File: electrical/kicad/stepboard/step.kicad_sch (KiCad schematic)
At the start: 80 parts, among them J1 Conn_02x03_Odd_Even, J10 Conn_02x03_Odd_Even, J11 Conn_02x03_Odd_Even, J12 Conn_02x03_Odd_Even, J13 Conn_01x04, J14 Conn_01x04, J15 Conn_01x04, J16 Conn_01x04, J17 Conn_02x03_Odd_Even, J18 Conn_02x03_Odd_Even, J19 Conn_02x03_Odd_Even, J2 Conn_02x03_Odd_Even, J20 Conn_02x03_Odd_Even, J21 Conn_01x04, J22 Conn_01x04, J23 Conn_01x04, J24 Conn_01x04, J25 Conn_02x12_Odd_Even, J26 Screw_Terminal_01x03, J3 Conn_02x03_Odd_Even, J4 Conn_02x03_Odd_Even, J5 Conn_01x04, J6 Conn_01x04, J7 Conn_01x04, J8 Conn_01x04, J9 Conn_02x03_Odd_Even, U1 MKS_TMC2209, U10 MKS_TMC2209, U11 MKS_TMC2209, U12 MKS_TMC2209, U2 MKS_TMC2209, U3 MKS_TMC2209, U4 MKS_TMC2209, U5 MKS_TMC2209, U6 MKS_TMC2209, U7 MKS_TMC2209, U8 MKS_TMC2209, U9 MKS_TMC2209

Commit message: update(kicad/pdb): sch with mobility components
- added rover mobility components to schematic
- added overcurrent and flyback protection ckt
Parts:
- renumbered J18 to J10, J19 to J11, J20 to J12, J5 to J13, J6 to J14, J7 to J15, J8 to J16, J13 to J17, J14 to J18, J15 to J19, J16 to J20, J9 to J5, J10 to J6, J11 to J7, J12 to J8, J17 to J9, R18 to R10, R19 to R11, R20 to R12, R5 to R13, R6 to R14, R7 to R15, R8 to R16, R13 to R17, R14 to R18, R15 to R19, R16 to R20, R9 to R5, R10 to R6, R11 to R7, R12 to R8, R17 to R9

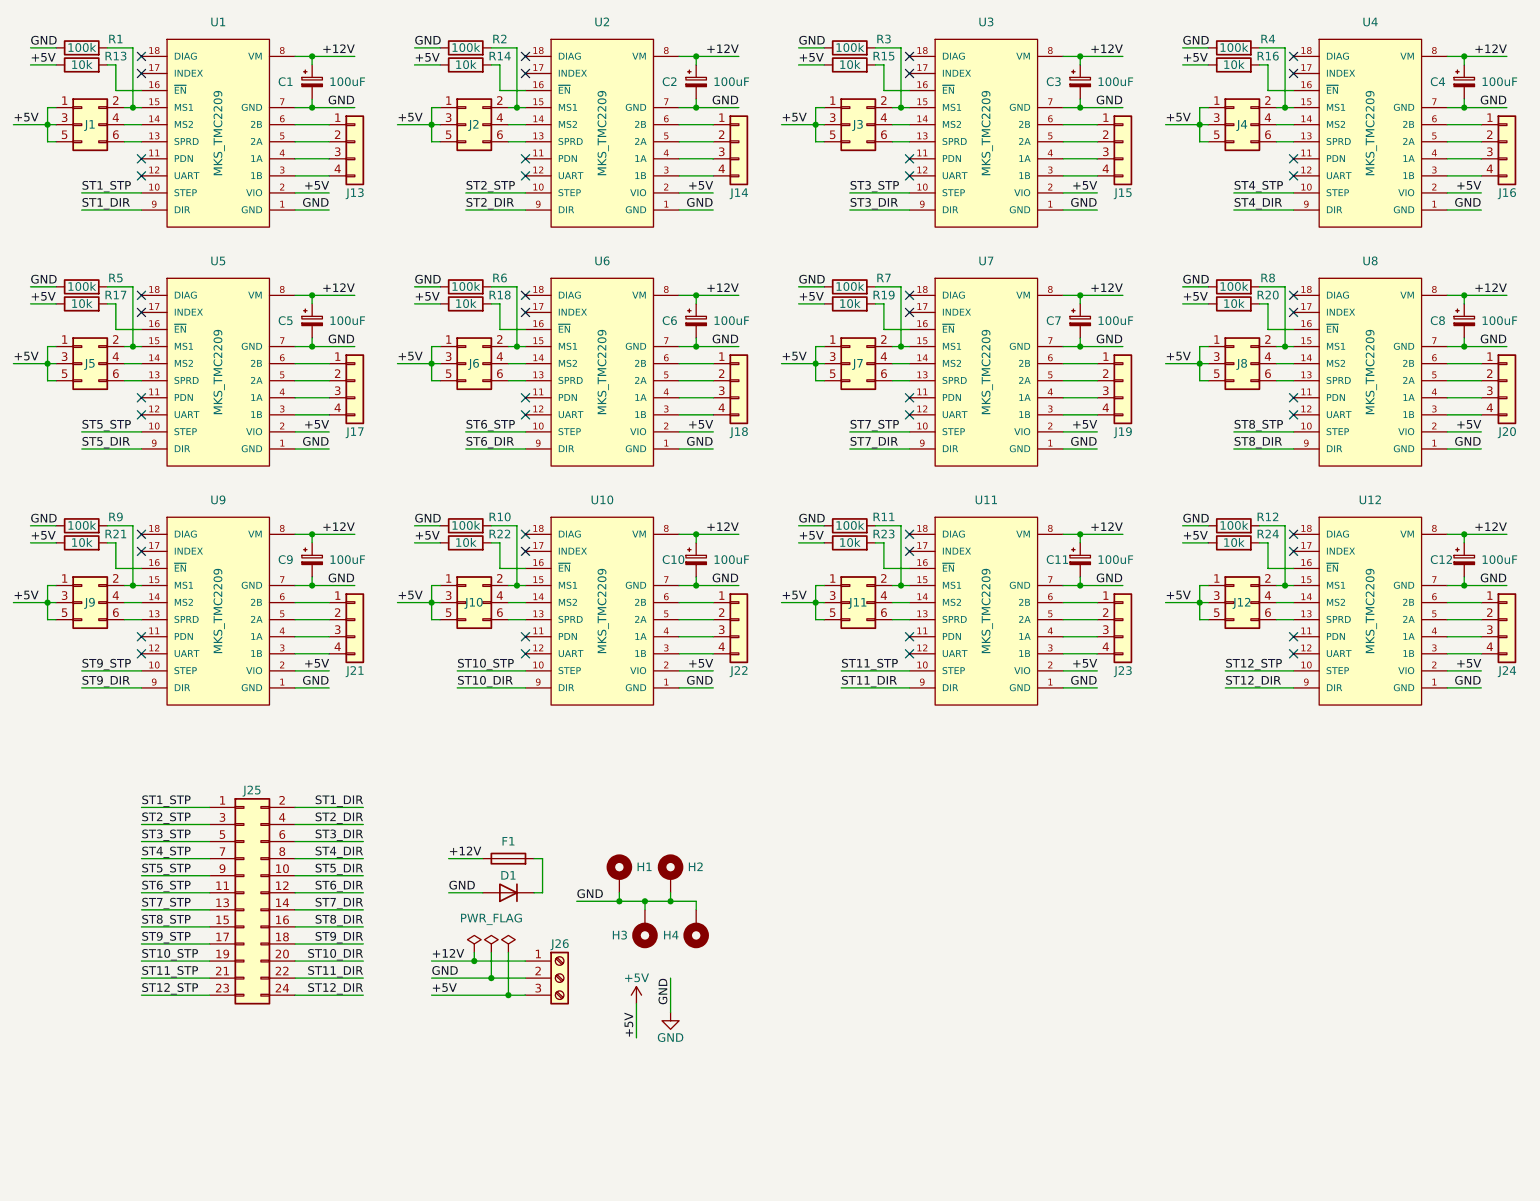
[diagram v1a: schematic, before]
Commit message: update(kicad/step): reduce from 12 to 9 motors and optimize space
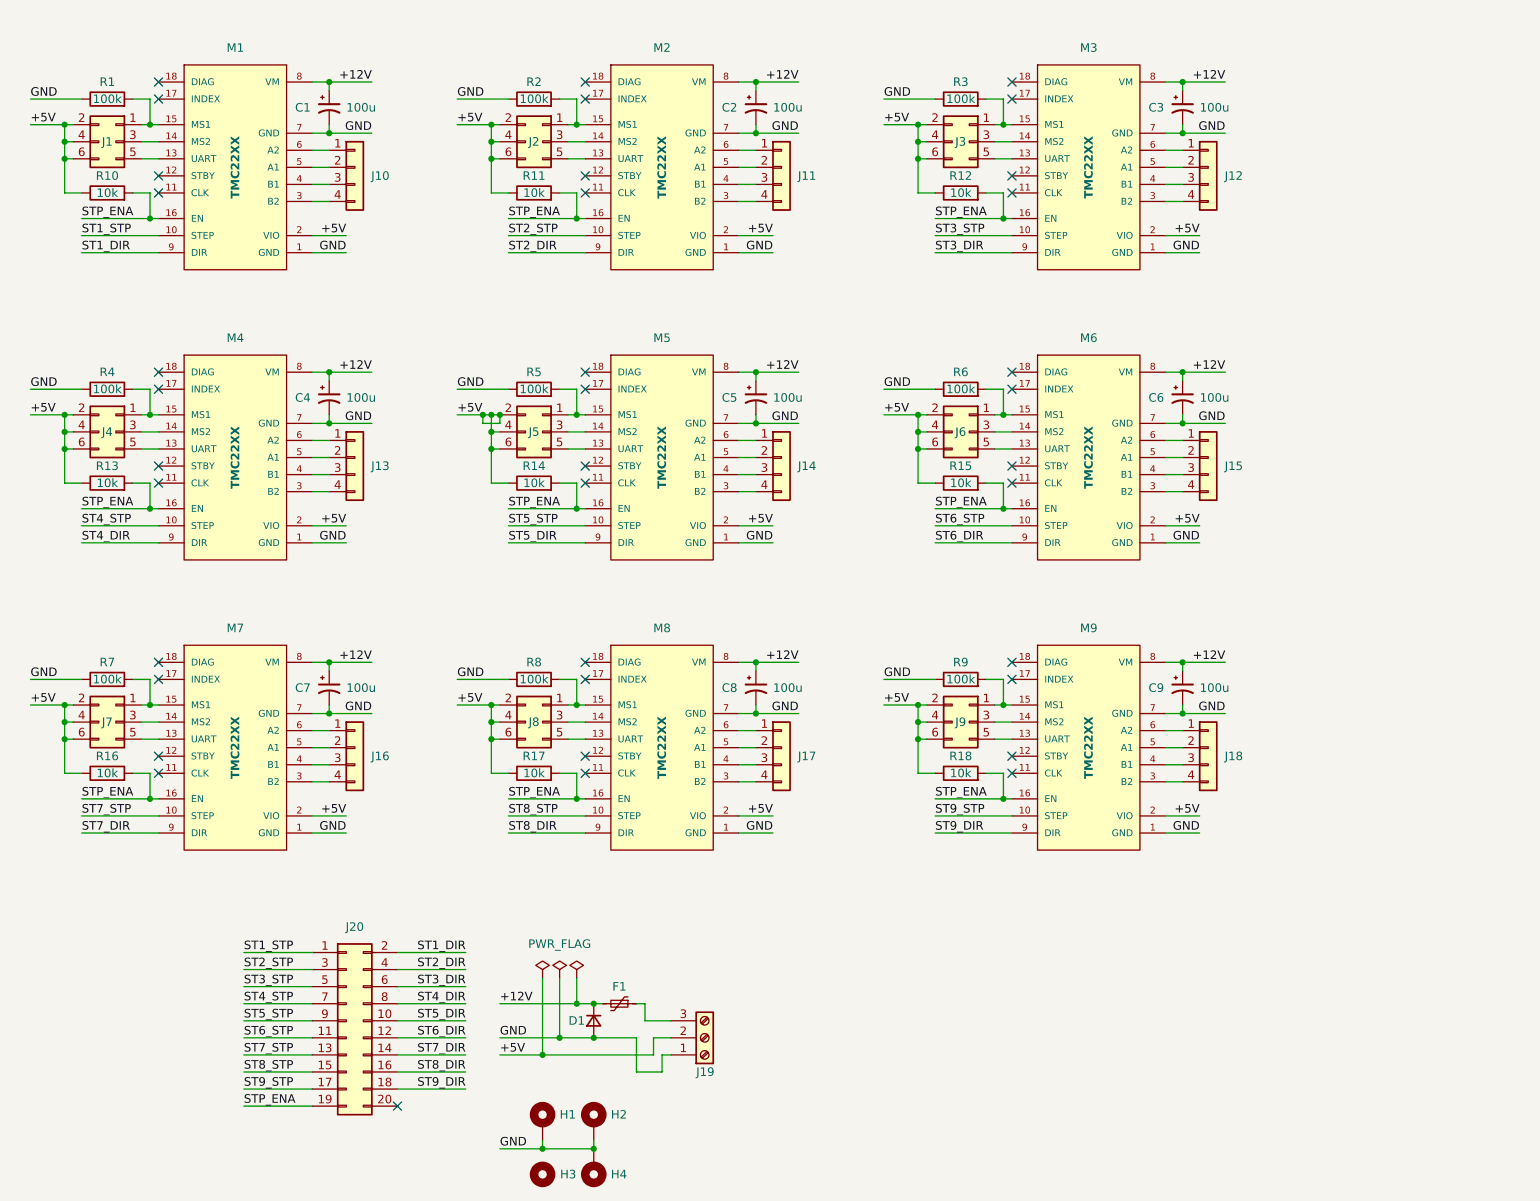
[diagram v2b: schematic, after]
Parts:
- removed C1, C10, C11, C12, C2, C3, C4, C5, C6, C7, C8, C9: 100uF, Capacitors_THT:CP_Radial_D8.0mm_P3.50mm_H12.0mm_Horizontal, symbol Device:C_Polarized_Small
- removed D1: D, Diode_THT:D_DO-35_SOD27_P7.62mm_Horizontal, symbol Device:D
- removed F1: Fuse, Fuses_THT:Fuse_Tyco-RUEF900, symbol Device:Fuse
- removed H3: MountingHole_Pad, MountingHole:MountingHole_3.2mm_M3_Pad_Via, symbol Mechanical:MountingHole_Pad
- removed J10, J11, J12: Conn_02x03_Odd_Even, Connector_PinHeader_2.54mm:PinHeader_2x03_P2.54mm_Vertical, symbol Connector_Generic:Conn_02x03_Odd_Even
- removed J19, J20, J21, J22, J23, J24: Conn_01x04, Connectors_JST:JST_XH_1x04_P2.54mm_Vertical, symbol Connector_Generic:Conn_01x04
- removed J25: Conn_02x12_Odd_Even, Connector_PinHeader_2.54mm:PinHeader_2x12_P2.54mm_Vertical, symbol Connector_Generic:Conn_02x12_Odd_Even
- removed R10: 100k, Resistor_THT:R_Axial_DIN0207_L6.3mm_D2.5mm_P7.62mm_Horizontal, symbol Device:R
- removed R19, R20, R21, R22, R23, R24: 10k, Resistor_THT:R_Axial_DIN0207_L6.3mm_D2.5mm_P7.62mm_Horizontal, symbol Device:R
- removed U1, U10, U11, U12, U2, U3, U4, U5, U6, U7, U8, U9: MKS_TMC2209, Motor_Driver:MKS_TMC2209, symbol Motor_Driver:TMC2209_Stepper_Driver
- added C1, C2, C3, C4, C5, C6, C7, C8, C9: 100u, Capacitor_THT:CP_Radial_D8.0mm_P2.50mm, symbol Device:C_Polarized_Small_US
- added D1: D_Small, Diode_THT:D_DO-35_SOD27_P7.62mm_Horizontal, symbol Device:D_Small
- added F1: Polyfuse_Small, Fuses_THT:Fuse_Tyco_RGEF1400, symbol Device:Polyfuse_Small
- added H3: MountingHole, MountingHole:MountingHole_3.2mm_M3, symbol Mechanical:MountingHole
- added J11, J12, J13: Conn_01x04, Connectors_JST:JST_XH_1x04_P2.54mm_Vertical, symbol Connector_Generic:Conn_01x04
- added J20: Conn_02x10_Odd_Even, Connector_PinHeader_2.54mm:PinHeader_2x10_P2.54mm_Vertical, symbol Connector_Generic:Conn_02x10_Odd_Even
- added M1, M2, M3, M4, M5, M6, M7, M8, M9: TMC22XX, Motor_Driver:MKS_TMC22XX, symbol Motor_Driver:TMC22XX
- added R13: 10k, Resistor_THT:R_Axial_DIN0204_L3.6mm_D1.6mm_P5.08mm_Horizontal, symbol Device:R
- J19: renamed from J26; footprint Connectors_JST:JST_XH_1x03_P2.54mm_Vertical -> Connector_Phoenix_MSTB:PhoenixContact_MSTBA_2,5_3-G-5,08_1x03_P5.08mm_Horizontal
- R1, R14, R15, R16, R17, R18, R2, R3, R4, R5, R6, R7, R8, R9: footprint Resistor_THT:R_Axial_DIN0207_L6.3mm_D2.5mm_P7.62mm_Horizontal -> Resistor_THT:R_Axial_DIN0204_L3.6mm_D1.6mm_P5.08mm_Horizontal
- R10: renamed from R13; footprint Resistor_THT:R_Axial_DIN0207_L6.3mm_D2.5mm_P7.62mm_Horizontal -> Resistor_THT:R_Axial_DIN0204_L3.6mm_D1.6mm_P5.08mm_Horizontal
- R11, R12: value 100k -> 10k; footprint Resistor_THT:R_Axial_DIN0207_L6.3mm_D2.5mm_P7.62mm_Horizontal -> Resistor_THT:R_Axial_DIN0204_L3.6mm_D1.6mm_P5.08mm_Horizontal
- renumbered J13 to J10
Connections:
- net +12V: now also C1.1, C2.1, C3.1, C4.1, C5.1, C6.1, C7.1, C8.1, C9.1, D1.1 (K), F1.2, M1.8 (VM), M2.8 (VM), M3.8 (VM), M4.8 (VM), M5.8 (VM), M6.8 (VM), M7.8 (VM), M8.8 (VM), M9.8 (VM); no longer J19.1 (Pin_1)
- net +5V: now also J1.2 (Pin_2), J1.4 (Pin_4), J1.6 (Pin_6), J19.2 (Pin_2), J2.2 (Pin_2), J2.4 (Pin_4), J2.6 (Pin_6), J3.2 (Pin_2), J3.4 (Pin_4), J3.6 (Pin_6), J4.2 (Pin_2), J4.4 (Pin_4), J4.6 (Pin_6), J5.2 (Pin_2), J5.4 (Pin_4), J5.6 (Pin_6), J6.2 (Pin_2), J6.4 (Pin_4), J6.6 (Pin_6), J7.2 (Pin_2), J7.4 (Pin_4), J7.6 (Pin_6), J8.2 (Pin_2), J8.4 (Pin_4), J8.6 (Pin_6), J9.2 (Pin_2), J9.4 (Pin_4), J9.6 (Pin_6), R11.1, R12.1, M1.2 (VIO), M2.2 (VIO), M3.2 (VIO), M4.2 (VIO), M5.2 (VIO), M6.2 (VIO), M7.2 (VIO), M8.2 (VIO), M9.2 (VIO), R13.1; no longer J1.1 (Pin_1), J1.3 (Pin_3), J1.5 (Pin_5), J19.3 (Pin_3), J2.1 (Pin_1), J2.3 (Pin_3), J2.5 (Pin_5), J3.1 (Pin_1), J3.3 (Pin_3), J3.5 (Pin_5), J4.1 (Pin_1), J4.3 (Pin_3), J4.5 (Pin_5), J5.1 (Pin_1), J5.3 (Pin_3), J5.5 (Pin_5), J6.1 (Pin_1), J6.3 (Pin_3), J6.5 (Pin_5), J7.1 (Pin_1), J7.3 (Pin_3), J7.5 (Pin_5), J8.1 (Pin_1), J8.3 (Pin_3), J8.5 (Pin_5), J9.1 (Pin_1), J9.3 (Pin_3), J9.5 (Pin_5)
- net GND: now also J19.1 (Pin_1), C1.2, C2.2, C3.2, C4.2, C5.2, C6.2, C7.2, C8.2, C9.2, D1.2 (A), M1.1 (GND), M1.7 (GND), M2.1 (GND), M2.7 (GND), M3.1 (GND), M3.7 (GND), M4.1 (GND), M4.7 (GND), M5.1 (GND), M5.7 (GND), M6.1 (GND), M6.7 (GND), M7.1 (GND), M7.7 (GND), M8.1 (GND), M8.7 (GND), M9.1 (GND), M9.7 (GND); no longer J19.2 (Pin_2), R11.1, R12.1
- net ST1_DIR: now also J20.2 (Pin_2), M1.9 (DIR)
- net ST1_STP: now also J20.1 (Pin_1), M1.10 (STEP)
- net ST2_DIR: now also J20.4 (Pin_4), M2.9 (DIR)
- net ST2_STP: now also J20.3 (Pin_3), M2.10 (STEP)
- net ST3_DIR: now also J20.6 (Pin_6), M3.9 (DIR)
- net ST3_STP: now also J20.5 (Pin_5), M3.10 (STEP)
- net ST4_DIR: now also J20.8 (Pin_8), M4.9 (DIR)
- net ST4_STP: now also J20.7 (Pin_7), M4.10 (STEP)
- net ST5_DIR: now also J20.10 (Pin_10), M5.9 (DIR)
- net ST5_STP: now also J20.9 (Pin_9), M5.10 (STEP)
- net ST6_DIR: now also J20.12 (Pin_12), M6.9 (DIR)
- net ST6_STP: now also J20.11 (Pin_11), M6.10 (STEP)
- net ST7_DIR: now also J20.14 (Pin_14), M7.9 (DIR)
- net ST7_STP: now also J20.13 (Pin_13), M7.10 (STEP)
- net ST8_DIR: now also J20.16 (Pin_16), M8.9 (DIR)
- net ST8_STP: now also J20.15 (Pin_15), M8.10 (STEP)
- net ST9_DIR: now also J20.18 (Pin_18), M9.9 (DIR)
- net ST9_STP: now also J20.17 (Pin_17), M9.10 (STEP)
- net STP_ENA: now reaches R11.2
- net STP_ENA: now also R10.2, R12.2, R14.2, R15.2, R16.2, R17.2, R18.2, J20.19 (Pin_19), M1.16 (EN), M2.16 (EN), M3.16 (EN), M4.16 (EN), M5.16 (EN), M6.16 (EN), M7.16 (EN), M8.16 (EN), M9.16 (EN), R13.2
- net at R8.2: now also J8.1 (Pin_1), M8.15 (MS1); no longer J8.2 (Pin_2)
- net at J14.1 (Pin_1): now also M5.6 (A2)
- net at J14.2 (Pin_2): now also M5.5 (A1)
- net at J14.3 (Pin_3): now also M5.4 (B1)
- net at J14.4 (Pin_4): now also M5.3 (B2)
- net at R5.2: now also J5.1 (Pin_1), M5.15 (MS1); no longer J5.2 (Pin_2)
- net at R9.2: now also J9.1 (Pin_1), M9.15 (MS1); no longer J9.2 (Pin_2)
- net at R7.2: now also J7.1 (Pin_1), M7.15 (MS1); no longer J7.2 (Pin_2)
- net at R2.2: now also J2.1 (Pin_1), M2.15 (MS1); no longer J2.2 (Pin_2)
- net at R3.2: now also J3.1 (Pin_1), M3.15 (MS1); no longer J3.2 (Pin_2)
- net at R6.2: now also J6.1 (Pin_1), M6.15 (MS1); no longer J6.2 (Pin_2)
- net at J18.4 (Pin_4): now also M9.3 (B2)
- net at J18.3 (Pin_3): now also M9.4 (B1)
- net at J18.2 (Pin_2): now also M9.5 (A1)
- net at J18.1 (Pin_1): now also M9.6 (A2)
- net at R1.2: now also J1.1 (Pin_1), M1.15 (MS1); no longer J1.2 (Pin_2)
- net at R4.2: now also J4.1 (Pin_1), M4.15 (MS1); no longer J4.2 (Pin_2)
- net at J17.4 (Pin_4): now also M8.3 (B2)
- net at J17.3 (Pin_3): now also M8.4 (B1)
- net at J17.2 (Pin_2): now also M8.5 (A1)
- net at J17.1 (Pin_1): now also M8.6 (A2)
- net at J16.1 (Pin_1): now also M7.6 (A2)
- net at J16.2 (Pin_2): now also M7.5 (A1)
- net at J16.3 (Pin_3): now also M7.4 (B1)
- net at J16.4 (Pin_4): now also M7.3 (B2)
- net at J15.4 (Pin_4): now also M6.3 (B2)
- net at J15.3 (Pin_3): now also M6.4 (B1)
- net at J15.2 (Pin_2): now also M6.5 (A1)
- net at J15.1 (Pin_1): now also M6.6 (A2)
- net at J10.4 (Pin_4): now also M1.3 (B2)
- net at J10.3 (Pin_3): now also M1.4 (B1)
- net at J10.2 (Pin_2): now also M1.5 (A1)
- net at J10.1 (Pin_1): now also M1.6 (A2)
- new net: J7.3 (Pin_3), M7.14 (MS2)
- new net: J7.5 (Pin_5), M7.13 (UART)
- new net: J8.3 (Pin_3), M8.14 (MS2)
- new net: J8.5 (Pin_5), M8.13 (UART)
- new net: J9.3 (Pin_3), M9.14 (MS2)
- new net: J9.5 (Pin_5), M9.13 (UART)
- new net: J12.1 (Pin_1), M3.6 (A2)
- new net: J12.2 (Pin_2), M3.5 (A1)
- new net: J12.3 (Pin_3), M3.4 (B1)
- new net: J12.4 (Pin_4), M3.3 (B2)
- new net: F1.1, J19.3 (Pin_3)
- new net: J13.1 (Pin_1), M4.6 (A2)
- new net: J13.2 (Pin_2), M4.5 (A1)
- new net: J13.3 (Pin_3), M4.4 (B1)
- new net: J13.4 (Pin_4), M4.3 (B2)
- new net: J2.3 (Pin_3), M2.14 (MS2)
- new net: J2.5 (Pin_5), M2.13 (UART)
- new net: J1.3 (Pin_3), M1.14 (MS2)
- new net: J1.5 (Pin_5), M1.13 (UART)
- new net: J5.5 (Pin_5), M5.13 (UART)
- new net: J5.3 (Pin_3), M5.14 (MS2)
- new net: J11.4 (Pin_4), M2.3 (B2)
- new net: J11.3 (Pin_3), M2.4 (B1)
- new net: J11.2 (Pin_2), M2.5 (A1)
- new net: J11.1 (Pin_1), M2.6 (A2)
- new net: J3.5 (Pin_5), M3.13 (UART)
- new net: J3.3 (Pin_3), M3.14 (MS2)
- new net: J6.3 (Pin_3), M6.14 (MS2)
- new net: J6.5 (Pin_5), M6.13 (UART)
- new net: J4.3 (Pin_3), M4.14 (MS2)
- new net: J4.5 (Pin_5), M4.13 (UART)
- no-connect marks 48 -> 37
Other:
- company: (none) -> Team RED
- title: (none) -> StepperBoard
- moved on the sheet: H1, H2, J10, J19, R1, R10
